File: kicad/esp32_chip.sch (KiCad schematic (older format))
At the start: 16 parts

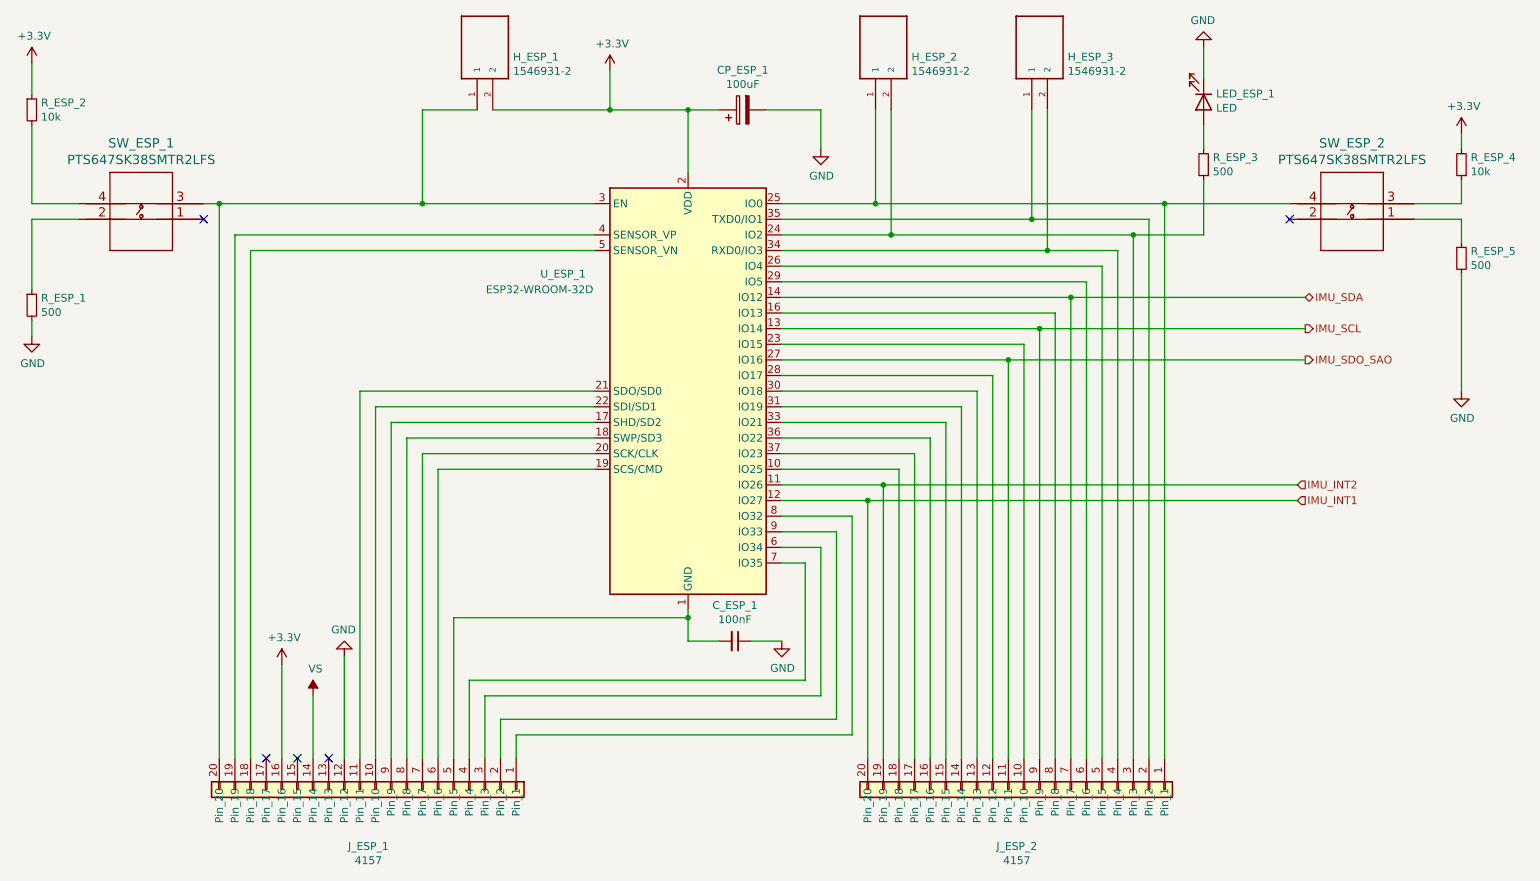
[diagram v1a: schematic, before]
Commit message: Created PCB design for ESP32 sensor for v0.0.1. Exported PDFs and gerber files
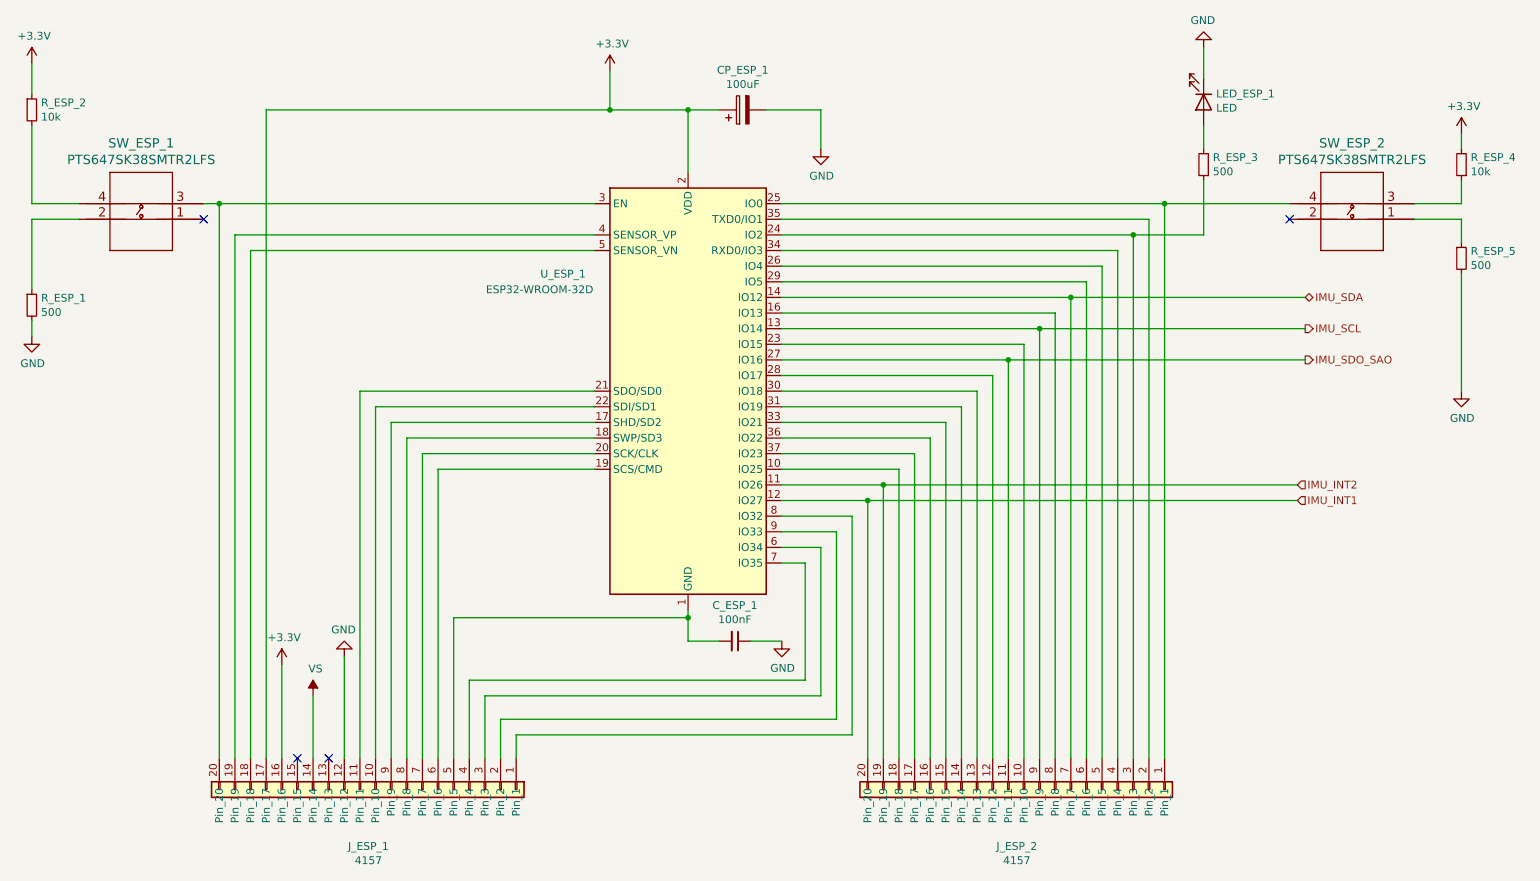
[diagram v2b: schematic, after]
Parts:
- removed H_ESP_1, H_ESP_2, H_ESP_3: 1546931-2, footprints:1546931-2, symbol 1546931-2:1546931-2
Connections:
- net +3V3: now also J_ESP_1.17 (Pin_17)
- no-connect marks 5 -> 4
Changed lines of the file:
@@
 Wire Wire Line
 	8150 2400 8150 5950
-$Comp
-L 1546931-2:1546931-2 H_ESP_3
-U 1 1 5FC1F433
-P 7400 1400
-F 0 "H_ESP_3" V 7339 1270 50  0000 R CNN
-F 1 "1546931-2" V 7248 1270 50  0000 R CNN
-F 2 "footprints:1546931-2" H 7400 1400 50  0001 L BNN
-F 3 "https://www.te.com/commerce/DocumentDelivery/DDEController?Action=srchrtrv&DocNm=1-1773458-1_EURO_STYLE_QRG&DocType=DS&DocLang=English" H 7400 1400 50  0001 L BNN
-F 4 "1546931-2" H 7400 1400 50  0001 C CNN "Part Name"
-F 5 "TE Connectivity AMP Connectors" H 7400 1400 50  0001 C CNN "Manufacturer"
-F 6 "Digikey Canada" H 7400 1400 50  0001 C CNN "Vendor"
-F 7 "" H 7400 1400 50  0001 C CNN "digikeypn"
-F 8 "A97965-ND" H 7400 1400 50  0001 C CNN "Vendor Part Name"
-	1    7400 1400
-	0    -1   -1   0
-$EndComp
-Wire Wire Line
-	5700 2500 7300 2500
-Wire Wire Line
-	7300 2500 7300 1800
-Wire Wire Line
-	7300 2500 8050 2500
 Wire Wire Line
 	8050 2500 8050 5950
-Connection ~ 7300 2500
-Wire Wire Line
-	5700 2600 6400 2600
 Wire Wire Line
 	7950 2600 7950 5950
 Wire Wire Line
-	7400 2700 7400 1800
-Wire Wire Line
-	5700 2700 7400 2700
-Wire Wire Line
-	7400 2700 7850 2700
-Wire Wire Line
 	7850 2700 7850 5950
-Connection ~ 7400 2700
 $Comp
 L Device:LED LED_ESP_1
@@
 	1    10150 2500
 	-1   0    0    1
-$EndComp
-$Comp
-L 1546931-2:1546931-2 H_ESP_1
-U 1 1 5FC3624B
-P 3850 1400
-F 0 "H_ESP_1" V 3789 1270 50  0000 R CNN
-F 1 "1546931-2" V 3698 1270 50  0000 R CNN
-F 2 "footprints:1546931-2" H 3850 1400 50  0001 L BNN
-F 3 "https://www.te.com/commerce/DocumentDelivery/DDEController?Action=srchrtrv&DocNm=1-1773458-1_EURO_STYLE_QRG&DocType=DS&DocLang=English" H 3850 1400 50  0001 L BNN
-F 4 "1546931-2" H 3850 1400 50  0001 C CNN "Part Name"
-F 5 "TE Connectivity AMP Connectors" H 3850 1400 50  0001 C CNN "Manufacturer"
-F 6 "Digikey Canada" H 3850 1400 50  0001 C CNN "Vendor"
-F 7 "" H 3850 1400 50  0001 C CNN "digikeypn"
-F 8 "A97965-ND" H 3850 1400 50  0001 C CNN "Vendor Part Name"
-	1    3850 1400
-	0    -1   -1   0
 $EndComp
 $Comp
@@
 Wire Wire Line
 	3000 3600 3000 5950
-Wire Wire Line
-	2100 2400 3400 2400
-Wire Wire Line
-	5700 2400 6300 2400
-Wire Wire Line
-	3400 2400 3400 1800
-Connection ~ 3400 2400
-Wire Wire Line
-	3400 2400 4500 2400
-$Comp
-L 1546931-2:1546931-2 H_ESP_2
-U 1 1 5FCBDB3B
-P 6400 1400
-F 0 "H_ESP_2" V 6339 1270 50  0000 R CNN
-F 1 "1546931-2" V 6248 1270 50  0000 R CNN
-F 2 "footprints:1546931-2" H 6400 1400 50  0001 L BNN
-F 3 "https://www.te.com/commerce/DocumentDelivery/DDEController?Action=srchrtrv&DocNm=1-1773458-1_EURO_STYLE_QRG&DocType=DS&DocLang=English" H 6400 1400 50  0001 L BNN
-F 4 "1546931-2" H 6400 1400 50  0001 C CNN "Part Name"
-F 5 "TE Connectivity AMP Connectors" H 6400 1400 50  0001 C CNN "Manufacturer"
-F 6 "Digikey Canada" H 6400 1400 50  0001 C CNN "Vendor"
-F 7 "" H 6400 1400 50  0001 C CNN "digikeypn"
-F 8 "A97965-ND" H 6400 1400 50  0001 C CNN "Vendor Part Name"
-	1    6400 1400
-	0    -1   -1   0
-$EndComp
 Connection ~ 5100 1800
 Wire Wire Line
-	3750 1800 3400 1800
-Wire Wire Line
 	5950 2050 5950 1800
-Wire Wire Line
-	6400 1800 6400 2600
-Connection ~ 6400 2600
-Wire Wire Line
-	6400 2600 7950 2600
-Wire Wire Line
-	6300 1800 6300 2400
-Connection ~ 6300 2400
-Wire Wire Line
-	6300 2400 8150 2400
 Wire Wire Line
 	10050 2400 10050 2250
@@
 	7150 3400 7150 5950
 Wire Wire Line
-	3850 1800 4600 1800
-Wire Wire Line
 	4600 1800 4600 1550
-Connection ~ 4600 1800
 Wire Wire Line
 	4600 1800 5100 1800
-$Comp
-L power:+3.3V #PWR0122
-U 1 1 5FDA2BCD
-P 2500 5350
-F 0 "#PWR0122" H 2500 5200 50  0001 C CNN
-F 1 "+3.3V" H 2515 5523 50  0000 C CNN
-F 2 "" H 2500 5350 50  0001 C CNN
-F 3 "" H 2500 5350 50  0001 C CNN
-	1    2500 5350
-	1    0    0    -1
-$EndComp
-$Comp
-L power:GND #PWR0123
-U 1 1 5FDF4623
-P 2900 5300
-F 0 "#PWR0123" H 2900 5050 50  0001 C CNN
-F 1 "GND" H 2905 5127 50  0000 C CNN
-F 2 "" H 2900 5300 50  0001 C CNN
-F 3 "" H 2900 5300 50  0001 C CNN
-	1    2900 5300
-	-1   0    0    1
-$EndComp
-$Comp
-L power:VS #PWR0124
-U 1 1 5FDF5FF7
-P 2700 5550
-F 0 "#PWR0124" H 2500 5400 50  0001 C CNN
-F 1 "VS" H 2715 5723 50  0000 C CNN
-F 2 "" H 2700 5550 50  0001 C CNN
-F 3 "" H 2700 5550 50  0001 C CNN
-	1    2700 5550
-	1    0    0    -1
-$EndComp
-Wire Wire Line
-	2500 5350 2500 5950
-Wire Wire Line
-	2700 5550 2700 5950
-Wire Wire Line
-	2900 5950 2900 5300
-NoConn ~ 2400 5950
 NoConn ~ 2600 5950
 NoConn ~ 2800 5950
@@
 Wire Wire Line
 	5500 5200 5700 5200
+Wire Wire Line
+	5700 2600 7950 2600
+Wire Wire Line
+	5700 2400 8150 2400
+Wire Wire Line
+	5700 2500 8050 2500
+Wire Wire Line
+	5700 2700 7850 2700
+Wire Wire Line
+	2100 2400 4500 2400
+Wire Wire Line
+	4600 1800 2400 1800
+Wire Wire Line
+	2400 1800 2400 5950
+Connection ~ 4600 1800
+Wire Wire Line
+	2500 5350 2500 5950
+Wire Wire Line
+	2700 5550 2700 5950
+Wire Wire Line
+	2900 5950 2900 5300
+$Comp
+L power:GND #PWR0123
+U 1 1 5FDF4623
+P 2900 5300
+F 0 "#PWR0123" H 2900 5050 50  0001 C CNN
+F 1 "GND" H 2905 5127 50  0000 C CNN
+F 2 "" H 2900 5300 50  0001 C CNN
+F 3 "" H 2900 5300 50  0001 C CNN
+	1    2900 5300
+	-1   0    0    1
+$EndComp
+$Comp
+L power:VS #PWR0124
+U 1 1 5FDF5FF7
+P 2700 5550
+F 0 "#PWR0124" H 2500 5400 50  0001 C CNN
+F 1 "VS" H 2715 5723 50  0000 C CNN
+F 2 "" H 2700 5550 50  0001 C CNN
+F 3 "" H 2700 5550 50  0001 C CNN
+	1    2700 5550
+	1    0    0    -1
+$EndComp
+$Comp
+L power:+3.3V #PWR0122
+U 1 1 5FDA2BCD
+P 2500 5350
+F 0 "#PWR0122" H 2500 5200 50  0001 C CNN
+F 1 "+3.3V" H 2515 5523 50  0000 C CNN
+F 2 "" H 2500 5350 50  0001 C CNN
+F 3 "" H 2500 5350 50  0001 C CNN
+	1    2500 5350
+	1    0    0    -1
+$EndComp
 $EndSCHEMATC

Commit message: Updated schematic and PCB design to v0.0.2 for 2-layer pcb. Added more silkscreen text
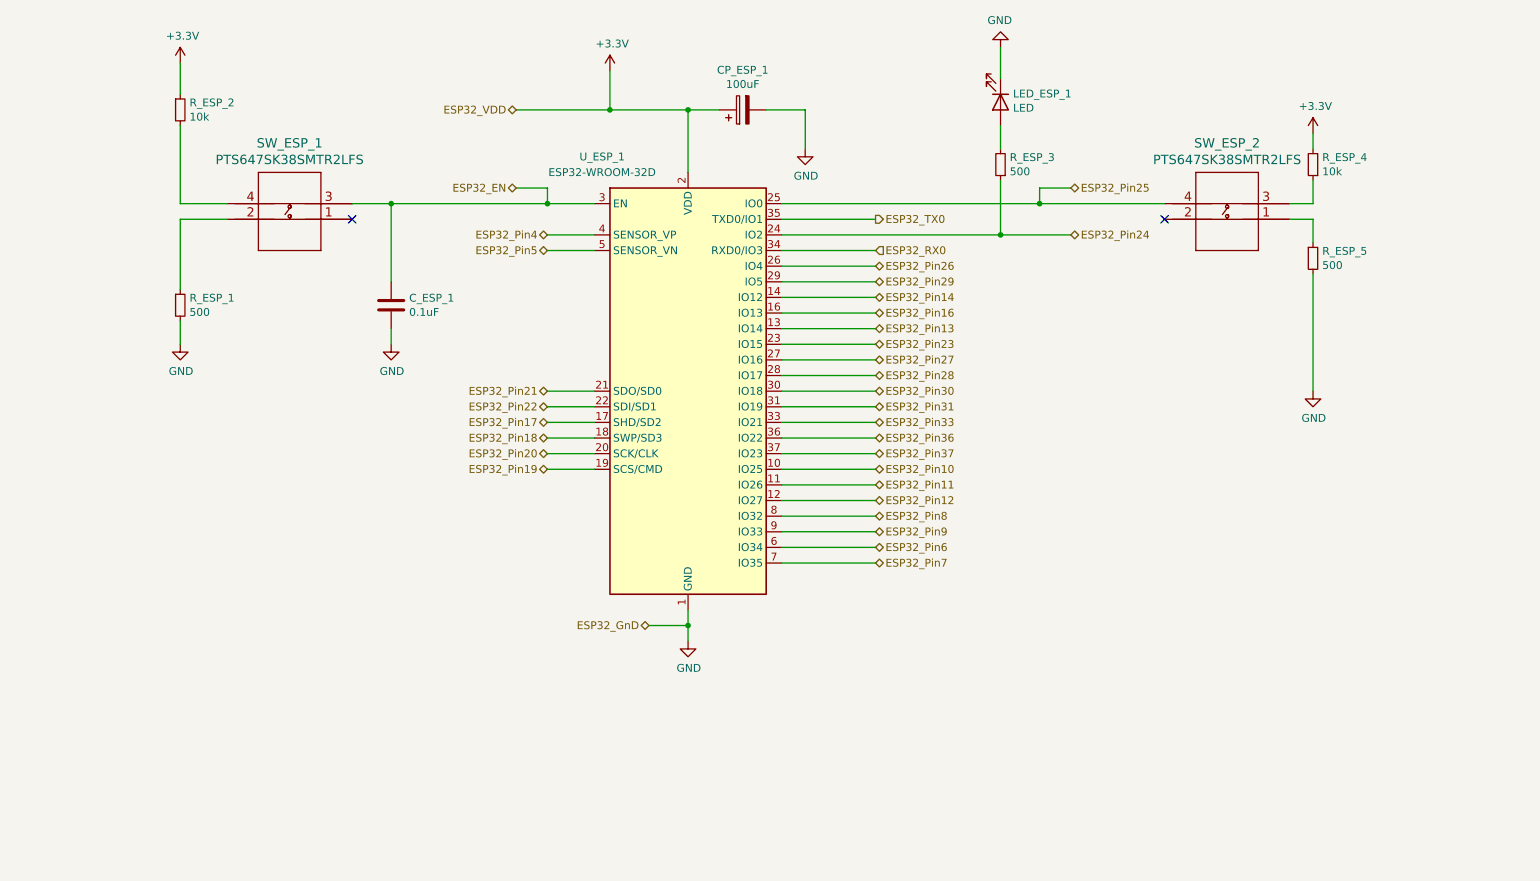
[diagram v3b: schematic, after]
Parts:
- removed C_ESP_1: 100nF, footprints:CAPC1608X90N, symbol Device:C_Small
- removed J_ESP_1, J_ESP_2: 4157, Connector_PinSocket_2.54mm:PinSocket_1x20_P2.54mm_Vertical, symbol CANtech:4157
- added C_ESP_1: 0.1uF, footprints:CAPC1608X90, symbol Device:C
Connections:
- net GND: now also U_ESP_1.1 (GND), U_ESP_1.15 (GND), U_ESP_1.38 (GND), U_ESP_1.39 (GND), C_ESP_1.2
- net ESP32_Pin10: now reaches U_ESP_1.10 (IO25)
- net ESP32_Pin16: now reaches U_ESP_1.16 (IO13)
- net ESP32_Pin17: now reaches U_ESP_1.17 (SHD/SD2)
- net ESP32_Pin18: now reaches U_ESP_1.18 (SWP/SD3)
- net ESP32_Pin19: now reaches U_ESP_1.19 (SCS/CMD)
- net ESP32_Pin20: now reaches U_ESP_1.20 (SCK/CLK)
- net ESP32_Pin21: now reaches U_ESP_1.21 (SDO/SD0)
- net ESP32_Pin22: now reaches U_ESP_1.22 (SDI/SD1)
- net ESP32_Pin23: now reaches U_ESP_1.23 (IO15)
- net ESP32_Pin24: now reaches R_ESP_3.1, U_ESP_1.24 (IO2)
- net ESP32_Pin25: now reaches SW_ESP_2.4, U_ESP_1.25 (IO0)
- net ESP32_Pin26: now reaches U_ESP_1.26 (IO4)
- net ESP32_Pin28: now reaches U_ESP_1.28 (IO17)
- net ESP32_Pin29: now reaches U_ESP_1.29 (IO5)
- net ESP32_EN: now reaches SW_ESP_1.3, U_ESP_1.3 (EN)
- net ESP32_EN: now also C_ESP_1.1
- net ESP32_Pin30: now reaches U_ESP_1.30 (IO18)
- net ESP32_Pin31: now reaches U_ESP_1.31 (IO19)
- net ESP32_Pin33: now reaches U_ESP_1.33 (IO21)
- net ESP32_RX0: now reaches U_ESP_1.34 (RXD0/IO3)
- net ESP32_TX0: now reaches U_ESP_1.35 (TXD0/IO1)
- net ESP32_Pin36: now reaches U_ESP_1.36 (IO22)
- net ESP32_Pin37: now reaches U_ESP_1.37 (IO23)
- net ESP32_Pin4: now reaches U_ESP_1.4 (SENSOR_VP)
- net ESP32_Pin5: now reaches U_ESP_1.5 (SENSOR_VN)
- net ESP32_Pin6: now reaches U_ESP_1.6 (IO34)
- net ESP32_Pin7: now reaches U_ESP_1.7 (IO35)
- net ESP32_Pin8: now reaches U_ESP_1.8 (IO32)
- net ESP32_Pin9: now reaches U_ESP_1.9 (IO33)
- net IMU_INT1 renamed ESP32_Pin12
- net IMU_INT2 renamed ESP32_Pin11
- net IMU_SCL renamed ESP32_Pin13
- net IMU_SDA renamed ESP32_Pin14
- net IMU_SDO_SAO renamed ESP32_Pin27
- no-connect marks 4 -> 2
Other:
- moved on the sheet: LED_ESP_1, R_ESP_1, R_ESP_2, R_ESP_3, R_ESP_4, R_ESP_5, SW_ESP_1, SW_ESP_2
